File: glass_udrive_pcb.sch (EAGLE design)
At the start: 24 parts

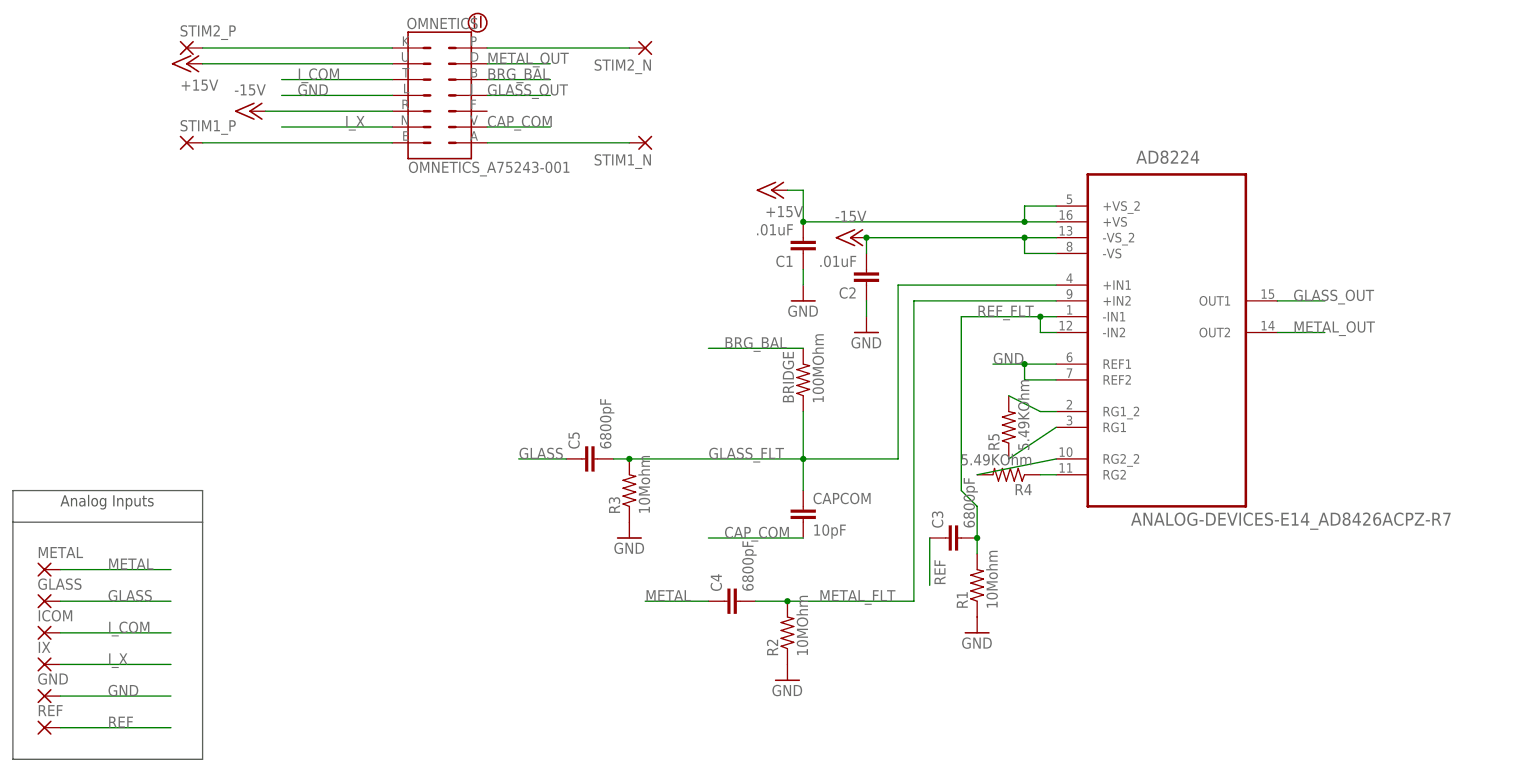
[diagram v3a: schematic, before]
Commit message: the modified version w/o output channel 2 and metal electrode input.
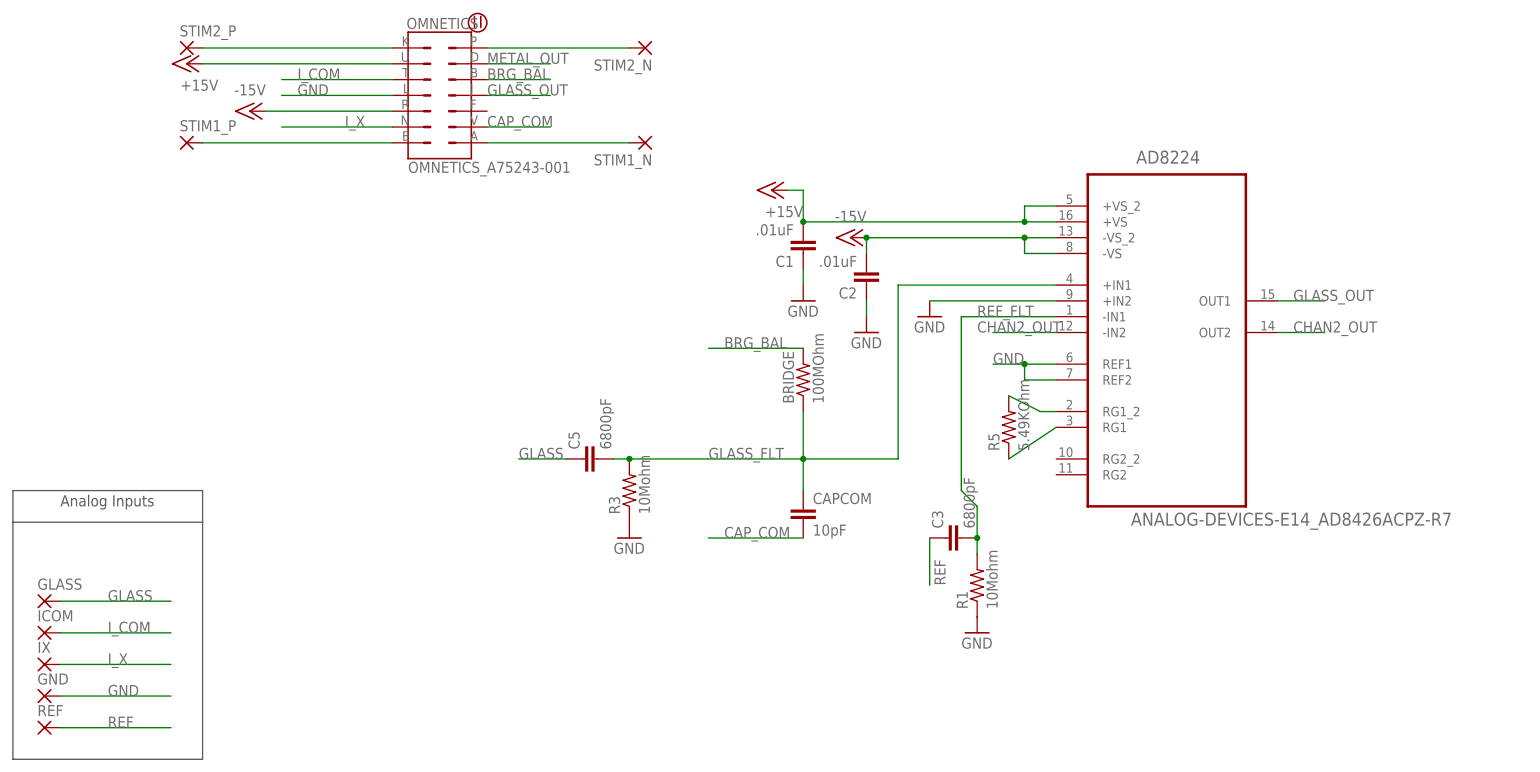
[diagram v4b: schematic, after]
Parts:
- removed C4: 6800pF, GFL:C_0201
- removed METAL: (no value), GFL:THROUGH-HOLE-30MIL/15MIL
- removed R2: 10MOhm, GFL:R_0201
- removed R4: 5.49KOhm, GFL:R_0201
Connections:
- removed net METAL: C4.1, METAL.P
- removed net METAL_FLT: AD8224.+IN2, C4.2, R2.2
- removed net N$6: AD8224.RG2_2, R4.2
- removed net N$8: AD8224.RG2, R4.1
- new net CHAN2_OUT: AD8224.-IN2, AD8224.OUT2
- net GND: now also AD8224.+IN2; no longer R2.1
- net METAL_OUT: no longer AD8224.OUT2
- net REF_FLT: no longer AD8224.-IN2
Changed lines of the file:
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@@
 <part name="REF" library="GFL" deviceset="THROUGH-HOLE-30MIL/15MIL" device=""/>
 <part name="R5" library="GFL" deviceset="R" device="_0201" value="5.49KOhm"/>
-<part name="R4" library="GFL" deviceset="R" device="_0201" value="5.49KOhm"/>
-<part name="METAL" library="GFL" deviceset="THROUGH-HOLE-30MIL/15MIL" device=""/>
 <part name="R3" library="GFL" deviceset="R" device="_0201" value="10Mohm"/>
-<part name="R2" library="GFL" deviceset="R" device="_0201" value="10MOhm"/>
 <part name="C5" library="GFL" deviceset="C" device="_0201" value="6800pF"/>
-<part name="C4" library="GFL" deviceset="C" device="_0201" value="6800pF"/>
 <part name="GND3" library="supply1" deviceset="GND" device=""/>
 <part name="GND4" library="supply1" deviceset="GND" device=""/>
@@
 <instance part="REF" gate="P" x="-5.08" y="15.24"/>
 <instance part="R5" gate="R" x="149.86" y="63.5" rot="R90"/>
-<instance part="R4" gate="R" x="149.86" y="55.88" rot="R180"/>
-<instance part="METAL" gate="P" x="-5.08" y="40.64"/>
 <instance part="R3" gate="R" x="88.9" y="53.34" rot="R90"/>
-<instance part="R2" gate="R" x="114.3" y="30.48" rot="R90"/>
 <instance part="C5" gate="C" x="81.28" y="58.42" rot="R90"/>
-<instance part="C4" gate="C" x="104.14" y="35.56" rot="R90"/>
-<instance part="GND3" gate="1" x="114.3" y="22.86"/>
+<instance part="GND3" gate="1" x="137.16" y="81.28"/>
 <instance part="GND4" gate="1" x="88.9" y="45.72"/>
 <instance part="R1" gate="R" x="144.78" y="38.1" rot="R90"/>
@@
 </segment>
 <segment>
-<pinref part="R2" gate="R" pin="1"/>
-<pinref part="GND3" gate="1" pin="GND"/>
-</segment>
-<segment>
 <pinref part="R1" gate="R" pin="1"/>
 <pinref part="GND5" gate="1" pin="GND"/>
+</segment>
+<segment>
+<pinref part="AD8224" gate="A" pin="+IN2"/>
+<pinref part="GND3" gate="1" pin="GND"/>
+<wire x1="157.48" y1="83.82" x2="137.16" y2="83.82" width="0.1524" layer="91"/>
 </segment>
 </net>
@@
 </segment>
 </net>
-<net name="N$6" class="0">
-<segment>
-<pinref part="AD8224" gate="A" pin="RG2_2"/>
-<pinref part="R4" gate="R" pin="2"/>
-<wire x1="157.48" y1="58.42" x2="144.78" y2="55.88" width="0.1524" layer="91"/>
-</segment>
-</net>
-<net name="N$8" class="0">
-<segment>
-<pinref part="AD8224" gate="A" pin="RG2"/>
-<pinref part="R4" gate="R" pin="1"/>
-<wire x1="157.48" y1="55.88" x2="154.94" y2="55.88" width="0.1524" layer="91"/>
-</segment>
-</net>
 <net name="GLASS" class="0">
 <segment>
@@
 </segment>
 </net>
-<net name="METAL" class="0">
-<segment>
-<pinref part="METAL" gate="P" pin="P"/>
-<wire x1="-2.54" y1="40.64" x2="15.24" y2="40.64" width="0.1524" layer="91"/>
-<label x="5.08" y="40.64" size="1.778" layer="95"/>
-</segment>
-<segment>
-<pinref part="C4" gate="C" pin="1"/>
-<wire x1="101.6" y1="35.56" x2="91.44" y2="35.56" width="0.1524" layer="91"/>
-<label x="91.44" y="35.56" size="1.778" layer="95"/>
-</segment>
-</net>
 <net name="GLASS_OUT" class="0">
 <segment>
@@
 </net>
 <net name="METAL_OUT" class="0">
-<segment>
-<pinref part="AD8224" gate="A" pin="OUT2"/>
-<wire x1="193.04" y1="78.74" x2="200.66" y2="78.74" width="0.1524" layer="91"/>
-<label x="195.58" y="78.74" size="1.778" layer="95"/>
-</segment>
 <segment>
 <pinref part="OMNETICS" gate="G$1" pin="D"/>
@@
 </segment>
 </net>
-<net name="METAL_FLT" class="0">
-<segment>
-<pinref part="AD8224" gate="A" pin="+IN2"/>
-<wire x1="157.48" y1="83.82" x2="134.62" y2="83.82" width="0.1524" layer="91"/>
-<wire x1="134.62" y1="83.82" x2="134.62" y2="35.56" width="0.1524" layer="91"/>
-<wire x1="134.62" y1="35.56" x2="114.3" y2="35.56" width="0.1524" layer="91"/>
-<label x="119.38" y="35.56" size="1.778" layer="95"/>
-<pinref part="R2" gate="R" pin="2"/>
-<pinref part="C4" gate="C" pin="2"/>
-<wire x1="114.3" y1="35.56" x2="109.22" y2="35.56" width="0.1524" layer="91"/>
-<junction x="114.3" y="35.56"/>
-</segment>
-</net>
 <net name="REF_FLT" class="0">
 <segment>
-<wire x1="142.24" y1="81.28" x2="154.94" y2="81.28" width="0.1524" layer="91"/>
+<wire x1="142.24" y1="81.28" x2="157.48" y2="81.28" width="0.1524" layer="91"/>
 <label x="144.78" y="81.28" size="1.778" layer="95"/>
 <pinref part="AD8224" gate="A" pin="-IN1"/>
-<pinref part="AD8224" gate="A" pin="-IN2"/>
-<wire x1="154.94" y1="81.28" x2="157.48" y2="81.28" width="0.1524" layer="91"/>
-<wire x1="157.48" y1="78.74" x2="154.94" y2="78.74" width="0.1524" layer="91"/>
-<wire x1="154.94" y1="78.74" x2="154.94" y2="81.28" width="0.1524" layer="91"/>
-<junction x="154.94" y="81.28"/>
 <pinref part="C3" gate="C" pin="2"/>
 <wire x1="144.78" y1="45.72" x2="144.78" y2="50.8" width="0.1524" layer="91"/>
@@
 </segment>
 </net>
+<net name="CHAN2_OUT" class="0">
+<segment>
+<pinref part="AD8224" gate="A" pin="OUT2"/>
+<wire x1="193.04" y1="78.74" x2="200.66" y2="78.74" width="0.1524" layer="91"/>
+<label x="195.58" y="78.74" size="1.778" layer="95"/>
+</segment>
+<segment>
+<pinref part="AD8224" gate="A" pin="-IN2"/>
+<wire x1="147.32" y1="78.74" x2="157.48" y2="78.74" width="0.1524" layer="91"/>
+<label x="144.78" y="78.74" size="1.778" layer="95"/>
+</segment>
+</net>

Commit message: 1-Incorporating Michael Stetner's comments: ====================================================== 1. Move vias carrying output signals away from the corners of the AD8224. According to the datasheet (bottom of p. 22), vias should not be placed under the corners of the chip. 2. If you have enough space, add a 10 uF bypass capacitor on each supply, as suggested by the datasheet. These can be far from the AD8224. 3. Add a through hole for GND. This hole will be used during surgery to solder the ground wire that you put under the bird's skull. You already have one GND through hole, but that will be in use by the motor. 4. Remove the vias for +15V and -15V that are underneath the AD8224. Just run those two of the traces on the top side of the board. 5. Change capacitance of C1-C2 to 0.1 uF, per the datasheet 6. Remove the trace between the reference pads of the AD8224. This creates a loop in your ground, and loops pick up electromagnetic interference. 7. Add an orientation marker for the AD8224 on the silkscreen 8. On the bill of materials, fix the device name for the AD8224 (it says AD8424). 9. Increase the width of the traces for Ix, ICOM, +15V, and -15V. A wider trace will have a lower resistance, which is especially important for these traces that will be carrying the most current. ====================================================== 2-Redesigned and re-routed to match the available componenets' package sizes. 3-Added the headplate structure with thru-holes 4- fixed the dimension layer
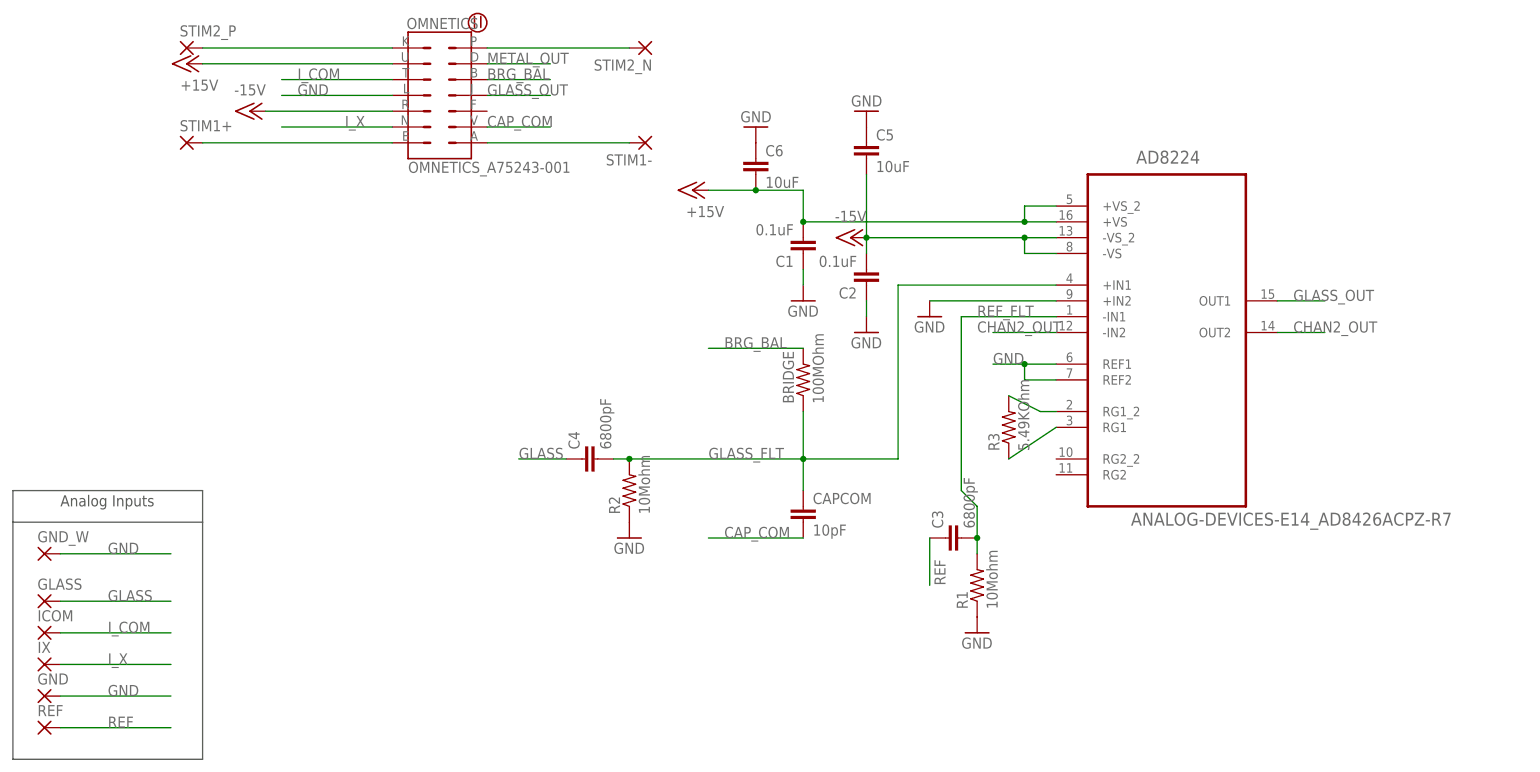
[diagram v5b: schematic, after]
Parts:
- removed R5: 5.49KOhm, GFL:R_0201
- added C4: 6800pF, GFL:C_0201
- added C6: 10uF, GFL:C_0603
- added GND_W: (no value), GFL:THROUGH-HOLE-30MIL/15MIL
- added R2: 10Mohm, GFL:R_0201
- BRIDGE: device GFL:R_0402 -> GFL:R_1206
- C1, C2: value .01uF -> 0.1uF
- C5: value 6800pF -> 10uF; device GFL:C_0201 -> GFL:C_0603
- R3: value 10Mohm -> 5.49KOhm
- renumbered STIM1_N to STIM1-, STIM1_P to STIM1+
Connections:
- net +15V: now also C6.2
- net -15V: now also C5.2
- net GLASS: now also C4.1; no longer C5.1
- net GLASS_FLT: now also C4.2, R2.2; no longer C5.2, R3.2
- net GND: now also C5.1, C6.1, GND_W.P, R2.1; no longer R3.1
- net N$2: now also R3.2; no longer R5.2
- net N$4: now also R3.1; no longer R5.1
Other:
- moved on the sheet: C5, R3
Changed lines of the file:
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@@
 <part name="FRAME1" library="frames" deviceset="LETTER_L" device=""/>
 <part name="OMNETICS" library="GFL" deviceset="OMNETICS_A75243-001" device=""/>
-<part name="BRIDGE" library="GFL" deviceset="R" device="_0402" value="100MOhm"/>
+<part name="BRIDGE" library="GFL" deviceset="R" device="_1206" value="100MOhm"/>
 <part name="CAPCOM" library="GFL" deviceset="C" device="_0402" value="10pF"/>
-<part name="C1" library="GFL" deviceset="C" device="_0201" value=".01uF"/>
-<part name="C2" library="GFL" deviceset="C" device="_0201" value=".01uF"/>
+<part name="C1" library="GFL" deviceset="C" device="_0201" value="0.1uF"/>
+<part name="C2" library="GFL" deviceset="C" device="_0201" value="0.1uF"/>
 <part name="P-1" library="supply1" deviceset="-15V" device=""/>
 <part name="P+1" library="supply1" deviceset="+15V" device=""/>
@@
 <part name="STIM2_N" library="GFL" deviceset="THROUGH-HOLE-30MIL/15MIL" device=""/>
 <part name="IX" library="GFL" deviceset="THROUGH-HOLE-30MIL/15MIL" device=""/>
-<part name="STIM1_N" library="GFL" deviceset="THROUGH-HOLE-30MIL/15MIL" device=""/>
-<part name="STIM1_P" library="GFL" deviceset="THROUGH-HOLE-30MIL/15MIL" device=""/>
+<part name="STIM1-" library="GFL" deviceset="THROUGH-HOLE-30MIL/15MIL" device=""/>
+<part name="STIM1+" library="GFL" deviceset="THROUGH-HOLE-30MIL/15MIL" device=""/>
 <part name="STIM2_P" library="GFL" deviceset="THROUGH-HOLE-30MIL/15MIL" device=""/>
 <part name="ICOM" library="GFL" deviceset="THROUGH-HOLE-30MIL/15MIL" device=""/>
@@
 <part name="AD8224" library="GyroDrive" deviceset="ANALOG-DEVICES-E14_AD8426ACPZ-R7" device=""/>
 <part name="REF" library="GFL" deviceset="THROUGH-HOLE-30MIL/15MIL" device=""/>
-<part name="R5" library="GFL" deviceset="R" device="_0201" value="5.49KOhm"/>
-<part name="R3" library="GFL" deviceset="R" device="_0201" value="10Mohm"/>
-<part name="C5" library="GFL" deviceset="C" device="_0201" value="6800pF"/>
+<part name="R3" library="GFL" deviceset="R" device="_0201" value="5.49KOhm"/>
+<part name="R2" library="GFL" deviceset="R" device="_0201" value="10Mohm"/>
+<part name="C4" library="GFL" deviceset="C" device="_0201" value="6800pF"/>
 <part name="GND3" library="supply1" deviceset="GND" device=""/>
 <part name="GND4" library="supply1" deviceset="GND" device=""/>
@@
 <part name="C3" library="GFL" deviceset="C" device="_0201" value="6800pF"/>
 <part name="GND5" library="supply1" deviceset="GND" device=""/>
+<part name="C6" library="GFL" deviceset="C" device="_0603" value="10uF"/>
+<part name="GND6" library="supply1" deviceset="GND" device=""/>
+<part name="C5" library="GFL" deviceset="C" device="_0603" value="10uF"/>
+<part name="GND7" library="supply1" deviceset="GND" device=""/>
+<part name="GND_W" library="GFL" deviceset="THROUGH-HOLE-30MIL/15MIL" device=""/>
 </parts>
 <sheets>
@@
 <instance part="C2" gate="C" x="127" y="86.36" rot="R180"/>
 <instance part="P-1" gate="1" x="124.46" y="93.98" rot="R270"/>
-<instance part="P+1" gate="1" x="111.76" y="101.6" rot="R90"/>
+<instance part="P+1" gate="1" x="99.06" y="101.6" rot="R90"/>
 <instance part="GND1" gate="1" x="116.84" y="83.82"/>
 <instance part="GND2" gate="1" x="127" y="78.74"/>
@@
 <instance part="STIM2_N" gate="P" x="91.44" y="124.46" rot="R180"/>
 <instance part="IX" gate="P" x="-5.08" y="25.4"/>
-<instance part="STIM1_N" gate="P" x="91.44" y="109.22" rot="R180"/>
-<instance part="STIM1_P" gate="P" x="17.78" y="109.22"/>
+<instance part="STIM1-" gate="P" x="91.44" y="109.22" rot="R180"/>
+<instance part="STIM1+" gate="P" x="17.78" y="109.22"/>
 <instance part="STIM2_P" gate="P" x="17.78" y="124.46"/>
 <instance part="ICOM" gate="P" x="-5.08" y="30.48"/>
@@
 <instance part="AD8224" gate="A" x="175.26" y="81.28"/>
 <instance part="REF" gate="P" x="-5.08" y="15.24"/>
-<instance part="R5" gate="R" x="149.86" y="63.5" rot="R90"/>
-<instance part="R3" gate="R" x="88.9" y="53.34" rot="R90"/>
-<instance part="C5" gate="C" x="81.28" y="58.42" rot="R90"/>
+<instance part="R3" gate="R" x="149.86" y="63.5" rot="R90"/>
+<instance part="R2" gate="R" x="88.9" y="53.34" rot="R90"/>
+<instance part="C4" gate="C" x="81.28" y="58.42" rot="R90"/>
 <instance part="GND3" gate="1" x="137.16" y="81.28"/>
 <instance part="GND4" gate="1" x="88.9" y="45.72"/>
@@
 <instance part="C3" gate="C" x="139.7" y="45.72" rot="R90"/>
 <instance part="GND5" gate="1" x="144.78" y="30.48"/>
+<instance part="C6" gate="C" x="109.22" y="106.68"/>
+<instance part="GND6" gate="1" x="109.22" y="111.76" rot="R180"/>
+<instance part="C5" gate="C" x="127" y="109.22"/>
+<instance part="GND7" gate="1" x="127" y="114.3" rot="R180"/>
+<instance part="GND_W" gate="P" x="-5.08" y="43.18"/>
 </instances>
 <busses>
@@
 <junction x="152.4" y="96.52"/>
 <pinref part="P+1" gate="1" pin="+15V"/>
-<wire x1="114.3" y1="101.6" x2="116.84" y2="101.6" width="0.1524" layer="91"/>
+<wire x1="101.6" y1="101.6" x2="109.22" y2="101.6" width="0.1524" layer="91"/>
+<wire x1="109.22" y1="101.6" x2="116.84" y2="101.6" width="0.1524" layer="91"/>
 <wire x1="116.84" y1="101.6" x2="116.84" y2="96.52" width="0.1524" layer="91"/>
 <junction x="116.84" y="96.52"/>
+<pinref part="C6" gate="C" pin="2"/>
+<junction x="109.22" y="101.6"/>
 </segment>
 </net>
@@
 <junction x="127" y="93.98"/>
 <wire x1="127" y1="93.98" x2="127" y2="91.44" width="0.1524" layer="91"/>
+<pinref part="C5" gate="C" pin="2"/>
+<wire x1="127" y1="93.98" x2="127" y2="104.14" width="0.1524" layer="91"/>
 </segment>
 </net>
@@
 </segment>
 <segment>
-<pinref part="R3" gate="R" pin="1"/>
+<pinref part="R2" gate="R" pin="1"/>
 <pinref part="GND4" gate="1" pin="GND"/>
 </segment>
@@
 <wire x1="157.48" y1="83.82" x2="137.16" y2="83.82" width="0.1524" layer="91"/>
 </segment>
+<segment>
+<pinref part="C6" gate="C" pin="1"/>
+<pinref part="GND6" gate="1" pin="GND"/>
+</segment>
+<segment>
+<pinref part="C5" gate="C" pin="1"/>
+<pinref part="GND7" gate="1" pin="GND"/>
+</segment>
+<segment>
+<pinref part="GND_W" gate="P" pin="P"/>
+<wire x1="-2.54" y1="43.18" x2="15.24" y2="43.18" width="0.1524" layer="91"/>
+<label x="5.08" y="43.18" size="1.778" layer="95"/>
+</segment>
 </net>
 <net name="CAP_COM" class="0">
@@
 <segment>
 <pinref part="OMNETICS" gate="G$1" pin="E"/>
-<pinref part="STIM1_P" gate="P" pin="P"/>
+<pinref part="STIM1+" gate="P" pin="P"/>
 <wire x1="50.8" y1="109.22" x2="20.32" y2="109.22" width="0.1524" layer="91"/>
 </segment>
@@
 <segment>
 <pinref part="OMNETICS" gate="G$1" pin="A"/>
-<pinref part="STIM1_N" gate="P" pin="P"/>
+<pinref part="STIM1-" gate="P" pin="P"/>
 <wire x1="66.04" y1="109.22" x2="88.9" y2="109.22" width="0.1524" layer="91"/>
 </segment>
@@
 <segment>
 <pinref part="AD8224" gate="A" pin="RG1_2"/>
-<pinref part="R5" gate="R" pin="2"/>
+<pinref part="R3" gate="R" pin="2"/>
 <wire x1="157.48" y1="66.04" x2="154.94" y2="66.04" width="0.1524" layer="91"/>
 <wire x1="154.94" y1="66.04" x2="149.86" y2="68.58" width="0.1524" layer="91"/>
@@
 <segment>
 <pinref part="AD8224" gate="A" pin="RG1"/>
-<pinref part="R5" gate="R" pin="1"/>
+<pinref part="R3" gate="R" pin="1"/>
 <wire x1="157.48" y1="63.5" x2="149.86" y2="58.42" width="0.1524" layer="91"/>
 </segment>
@@
 </segment>
 <segment>
-<pinref part="C5" gate="C" pin="1"/>
+<pinref part="C4" gate="C" pin="1"/>
 <wire x1="78.74" y1="58.42" x2="71.12" y2="58.42" width="0.1524" layer="91"/>
 <label x="71.12" y="58.42" size="1.778" layer="95"/>
@@
 <pinref part="AD8224" gate="A" pin="+IN1"/>
 <wire x1="132.08" y1="86.36" x2="157.48" y2="86.36" width="0.1524" layer="91"/>
-<pinref part="R3" gate="R" pin="2"/>
+<pinref part="R2" gate="R" pin="2"/>
 <wire x1="88.9" y1="58.42" x2="86.36" y2="58.42" width="0.1524" layer="91"/>
 <junction x="88.9" y="58.42"/>
-<pinref part="C5" gate="C" pin="2"/>
-</segment>
-</net>
+<pinref part="C4" gate="C" pin="2"/>
+</segment>
+</net>
